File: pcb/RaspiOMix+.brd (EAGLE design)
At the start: 65 x 56 mm, 103 parts, among them IC3 DS1307, IC4 MCP3424-E/ST, IC5 MCP3424-E/ST, IC6 TMP101, K1 PIN20X2, U1 EEPROM24

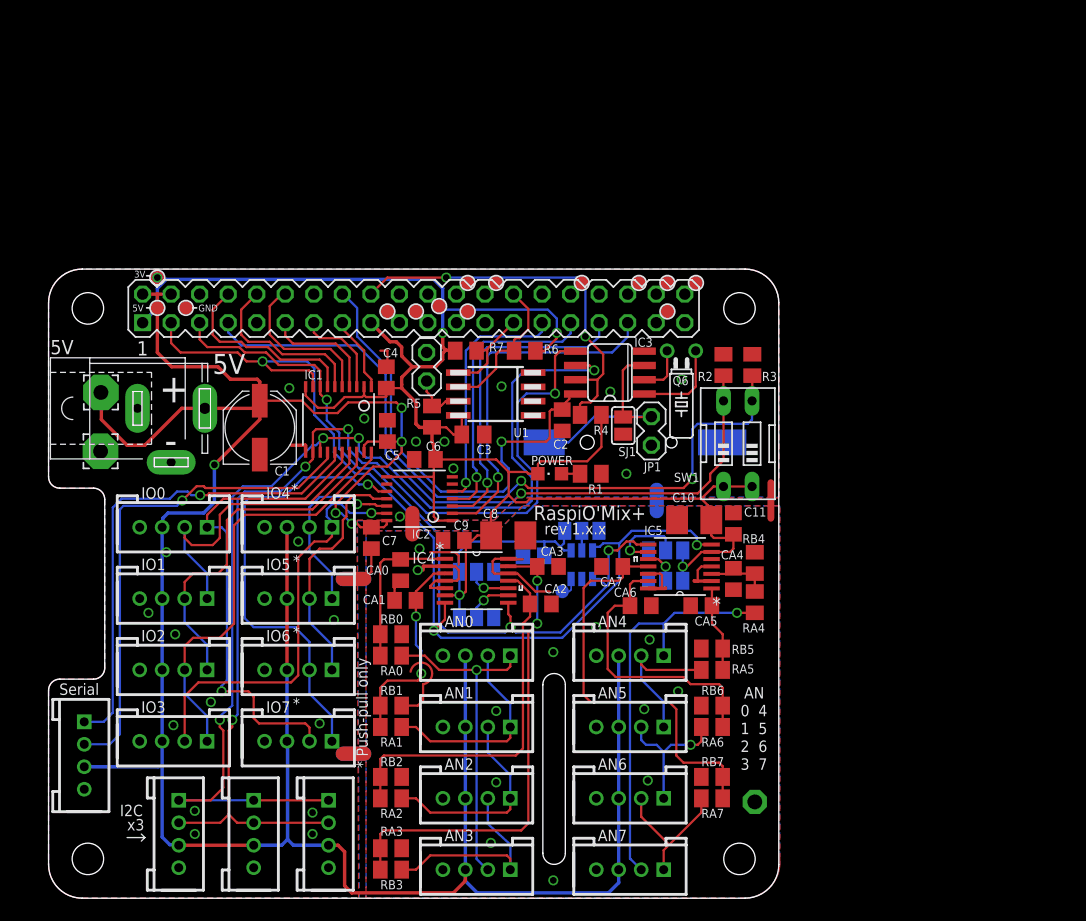
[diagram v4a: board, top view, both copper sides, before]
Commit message: RaspiO'Mix+ -> Pcb 2.0.0
New RaspiO’Mix+ pcbs version is 2.0.0.
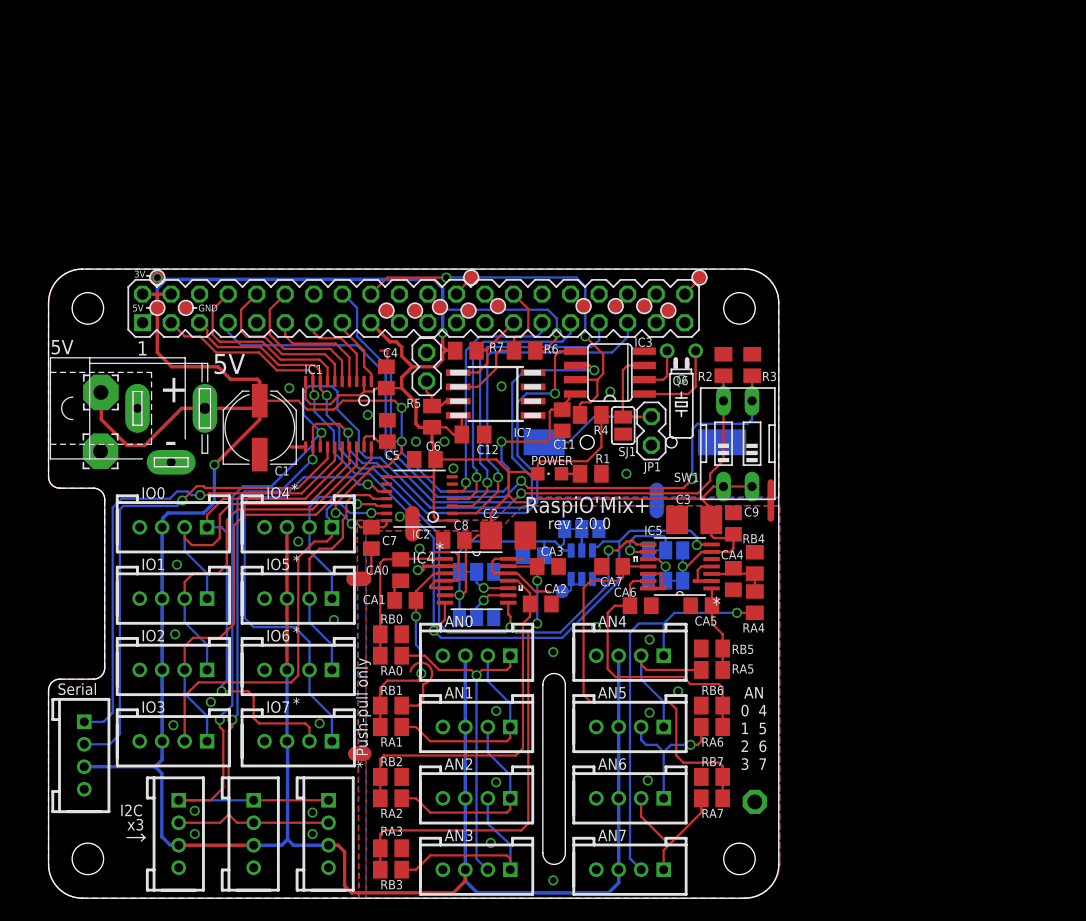
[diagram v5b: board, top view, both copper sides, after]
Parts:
- C10, C8: value (none) -> 100nf; device rcl:B/3528-21R -> rcl:C0805
- C12: device rcl:C0805 -> resistor:C0805K
- C2: value 100nf -> 1uf; device rcl:C0805 -> rcl:B/3528-21R
- C3: value 100nF -> 1uf; device resistor:C0805K -> rcl:B/3528-21R
- IC1: value (none) -> TXS0108PWR
- IC2: value (none) -> TXB0104PWR
- Q6: value (none) -> 32.768khz
- moved C9 24.9 mm to (61.0, 33.3), turned to 270 degrees
- moved C3 21.1 mm to (57.5, 33.7)
- moved C11 17.8 mm to (45.7, 42.5)
- moved C10 14.6 mm to (43.2, 30.5), flipped to the bottom
- moved C12 12.1 mm to (37.8, 41.3), flipped to the top
- moved C2 11.3 mm to (40.9, 32.3), turned to 180 degrees
- moved C8 4.87 mm to (36.1, 31.8), turned to 0 degrees
- moved TP3 2.92 mm to (53.0, 52.7)
- moved TP4 2.92 mm to (50.5, 52.7)
- moved TP9 2.07 mm to (40.0, 52.7)
- moved TP5 2.07 mm to (47.6, 52.7)
- moved TP2 0.57 mm to (57.9, 55.2)
- moved TP8 0.57 mm to (37.6, 55.2)
- moved IC1 0.48 mm to (25.8, 43.1)
- moved J_ADR4 0.16 mm to (47.5, 32.9)
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- renumbered U1 to IC7
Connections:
- net +3V3: now also C10.1, C2.+, C3.+, C8.2; no longer C10.+, C11.2, C3.1, C8.+
- net +5V: now also C11.1; no longer C2.1
- net VSS: now also C10.2, C11.2, C2.-, C3.-, C8.1; no longer C10.-, C11.1, C2.2, C3.2, C8.-
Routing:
- net SCL: track 99.1 -> 108.4 mm, vias 4 -> 3
- net PI_SDA: track 87.6 -> 80.3 mm
- net VSS: track 59.1 -> 54.6 mm, vias 34 -> 33
- net N$28: track 0.00 -> 0.79 mm
- net N$27: track 0.00 -> 0.79 mm
- net PI_RX: track 15.6 -> 15.0 mm
- net PI_IO0: track 14.1 -> 13.4 mm
- net N$23: track 0.00 -> 0.64 mm
- net N$26: track 0.00 -> 0.63 mm
- net N$25: track 0.00 -> 0.63 mm
- net N$24: track 0.00 -> 0.63 mm
- net N$1: track 1.41 -> 2.02 mm
- net PI_SCL: track 69.4 -> 68.8 mm
- net N$16: track 1.41 -> 1.98 mm
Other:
- board text added: "rev 2.0.0"
- board text removed: "rev 1.x.x"

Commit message: Misc
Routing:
- net VSS: vias 33 -> 34
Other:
- board text added: "rev 2.0.1"
- board text removed: "rev 2.0.0"
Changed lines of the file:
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@@
 <text x="63.1825" y="13.0175" size="1.016" layer="21" font="vector">6</text>
 <text x="63.1825" y="11.43" size="1.016" layer="21" font="vector">7</text>
-<text x="44.45" y="32.86125" size="1.016" layer="21" font="vector">rev 2.0.0</text>
+<text x="44.45" y="32.86125" size="1.016" layer="21" font="vector">rev 2.0.1</text>
 <text x="31.59125" y="48.5775" size="1.4224" layer="26" font="vector" rot="MR0">www.digitalspirit.org</text>
 <text x="31.59125" y="46.355" size="1.27" layer="26" font="vector" rot="MR0">2014/11</text>
@@
 <circle x="57.94375" y="55.245" radius="0.654540625" width="0.1524" layer="21"/>
 <circle x="55.165625" y="52.308125" radius="0.654540625" width="0.1524" layer="21"/>
+<circle x="36.67125" y="30.00375" radius="0.15875" width="0.4064" layer="21"/>
+<circle x="57.62625" y="27.78125" radius="0.15875" width="0.4064" layer="21"/>
+<circle x="51.1175" y="45.085" radius="0.15875" width="0.4064" layer="21"/>
 </plain>
 <attributes>
@@
 </element>
 <element name="RA3" library="rcl" package="M0805" value="10k 0.1%" x="30.48" y="2.54" smashed="yes">
-<attribute name="NAME" x="29.5275" y="5.55625" size="0.8128" layer="25"/>
+<attribute name="NAME" x="29.36875" y="0.635" size="0.8128" layer="25"/>
 <attribute name="VALUE" x="29.21" y="0" size="1.27" layer="27"/>
 </element>
@@
 </element>
 <element name="RB3" library="rcl" package="M0805" value="6.8k 1%" x="30.48" y="4.445" smashed="yes" rot="R180">
-<attribute name="NAME" x="29.5275" y="0.79375" size="0.8128" layer="25" rot="R180" align="top-right"/>
+<attribute name="NAME" x="29.5275" y="5.55625" size="0.8128" layer="25" rot="R180" align="top-right"/>
 <attribute name="VALUE" x="31.75" y="6.985" size="1.27" layer="27" rot="R180"/>
 </element>
@@
 <wire x1="40.48125" y1="36.195" x2="40.9575" y2="36.67125" width="0.2032" layer="16"/>
 <wire x1="40.9575" y1="36.67125" x2="40.9575" y2="38.25875" width="0.2032" layer="16"/>
-<wire x1="40.9575" y1="38.25875" x2="40.3225" y2="38.89375" width="0.2032" layer="16"/>
-<wire x1="40.3225" y1="38.89375" x2="40.3225" y2="40.64" width="0.2032" layer="16"/>
-<via x="40.3225" y="40.64" extent="1-16" drill="0.6"/>
-<wire x1="40.3225" y1="40.64" x2="44.29125" y2="40.64" width="0.2032" layer="1"/>
+<wire x1="40.9575" y1="38.25875" x2="40.16375" y2="39.0525" width="0.2032" layer="16"/>
+<wire x1="40.16375" y1="39.0525" x2="40.16375" y2="40.64" width="0.2032" layer="16"/>
+<via x="40.16375" y="40.64" extent="1-16" drill="0.6"/>
+<wire x1="40.16375" y1="40.64" x2="44.29125" y2="40.64" width="0.2032" layer="1"/>
 <wire x1="44.29125" y1="40.64" x2="44.60875" y2="40.9575" width="0.2032" layer="1"/>
 <wire x1="44.60875" y1="40.9575" x2="44.60875" y2="43.33875" width="0.2032" layer="1"/>
@@
 <via x="13.0175" y="5.715" extent="1-16" drill="0.6"/>
 <via x="14.44625" y="17.4625" extent="1-16" drill="0.6"/>
+<via x="55.40375" y="26.3525" extent="1-16" drill="0.6"/>
 <wire x1="40.9194" y1="28.9179" x2="40.9575" y2="28.8925" width="0" layer="19" extent="1-1"/>
 <wire x1="39.624" y1="29.05125" x2="39.52875" y2="29.05125" width="0" layer="19" extent="1-16"/>
-<wire x1="53.3781" y1="28.8671" x2="53.4035" y2="28.2575" width="0" layer="19" extent="1-16"/>
 </signal>
 <signal name="SDA">
@@
 <wire x1="45.085" y1="44.92625" x2="42.545" y2="44.92625" width="0.2032" layer="16"/>
 <wire x1="42.545" y1="44.92625" x2="41.75125" y2="44.1325" width="0.2032" layer="16"/>
-<wire x1="41.75125" y1="44.1325" x2="41.75125" y2="39.37" width="0.2032" layer="16"/>
-<wire x1="41.75125" y1="39.37" x2="43.4975" y2="37.62375" width="0.2032" layer="16"/>
+<wire x1="41.75125" y1="44.1325" x2="41.75125" y2="42.38625" width="0.2032" layer="16"/>
+<wire x1="41.75125" y1="42.38625" x2="41.43375" y2="42.06875" width="0.2032" layer="16"/>
+<wire x1="41.43375" y1="42.06875" x2="41.43375" y2="39.6875" width="0.2032" layer="16"/>
+<wire x1="41.43375" y1="39.6875" x2="43.4975" y2="37.62375" width="0.2032" layer="16"/>
 <wire x1="43.4975" y1="37.62375" x2="43.4975" y2="35.2425" width="0.2032" layer="16"/>
 <wire x1="43.4975" y1="35.2425" x2="42.545" y2="34.29" width="0.2032" layer="16"/>
@@
 <wire x1="48.5775" y1="46.99" x2="42.38625" y2="46.99" width="0.2032" layer="16"/>
 <wire x1="42.38625" y1="46.99" x2="41.275" y2="45.87875" width="0.2032" layer="16"/>
-<wire x1="41.275" y1="45.87875" x2="41.275" y2="39.21125" width="0.2032" layer="16"/>
-<wire x1="41.275" y1="39.21125" x2="43.02125" y2="37.465" width="0.2032" layer="16"/>
+<wire x1="41.275" y1="45.87875" x2="41.275" y2="42.545" width="0.2032" layer="16"/>
+<wire x1="41.275" y1="42.545" x2="40.9575" y2="42.2275" width="0.2032" layer="16"/>
+<wire x1="40.9575" y1="42.2275" x2="40.9575" y2="41.5925" width="0.2032" layer="16"/>
+<wire x1="40.9575" y1="41.5925" x2="40.9575" y2="39.52875" width="0.2032" layer="16"/>
+<wire x1="40.9575" y1="39.52875" x2="43.02125" y2="37.465" width="0.2032" layer="16"/>
 <wire x1="43.02125" y1="37.465" x2="43.02125" y2="35.40125" width="0.2032" layer="16"/>
 <wire x1="43.02125" y1="35.40125" x2="42.38625" y2="34.76625" width="0.2032" layer="16"/>

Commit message: PCB Version 2.0.2
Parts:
- moved C3 0.22 mm to (57.3, 33.8)
- moved C6 0.16 mm to (33.5, 39.2)
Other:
- board text added: "rev 2.0.2"
- board text removed: "rev 2.0.1"
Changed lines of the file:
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@@
 <?xml version="1.0" encoding="utf-8"?>
 <!DOCTYPE eagle SYSTEM "eagle.dtd">
-<eagle version="7.2.0">
+<eagle version="7.3.0">
 <drawing>
 <settings>
@@
 <text x="63.1825" y="13.0175" size="1.016" layer="21" font="vector">6</text>
 <text x="63.1825" y="11.43" size="1.016" layer="21" font="vector">7</text>
-<text x="44.45" y="32.86125" size="1.016" layer="21" font="vector">rev 2.0.1</text>
+<text x="44.45" y="32.86125" size="1.016" layer="21" font="vector">rev 2.0.2</text>
 <text x="31.59125" y="48.5775" size="1.4224" layer="26" font="vector" rot="MR0">www.digitalspirit.org</text>
 <text x="31.59125" y="46.355" size="1.27" layer="26" font="vector" rot="MR0">2014/11</text>
@@
 <text x="19.3675" y="0.635" size="1.016" layer="22" font="vector" rot="MR0">I2C</text>
 <text x="25.7175" y="0.635" size="1.016" layer="22" font="vector" rot="MR0">I2C</text>
-<text x="9.8425" y="2.2225" size="1.016" layer="22" font="vector" rot="MR0">SCL</text>
-<text x="9.8425" y="4.1275" size="1.016" layer="22" font="vector" rot="MR0">SDA</text>
+<text x="9.8425" y="8.255" size="1.016" layer="22" font="vector" rot="MR0">SCL</text>
+<text x="9.8425" y="6.35" size="1.016" layer="22" font="vector" rot="MR0">SDA</text>
 <text x="5.87375" y="13.335" size="1.016" layer="22" font="vector" rot="MR0">TX</text>
 <text x="5.87375" y="15.24" size="1.016" layer="22" font="vector" rot="MR0">RX</text>
@@
 <attribute name="VALUE" x="54.8274" y="30.95625" size="0.02" layer="28" rot="MR180"/>
 </element>
-<element name="C3" library="rcl" package="B/3528-21R" value="1uf" x="57.4675" y="33.655" smashed="yes">
-<attribute name="NAME" x="55.835" y="35.09625" size="0.8128" layer="25"/>
-<attribute name="VALUE" x="55.5175" y="30.73" size="1.27" layer="27"/>
+<element name="C3" library="rcl" package="B/3528-21R" value="1uf" x="57.30875" y="33.81375" smashed="yes">
+<attribute name="NAME" x="55.67625" y="35.255" size="0.8128" layer="25"/>
+<attribute name="VALUE" x="55.35875" y="30.88875" size="1.27" layer="27"/>
 </element>
 <element name="IC2" library="adafruit" package="TSSOP14" value="TXB0104PWR" x="33.02" y="35.56" smashed="yes" rot="R90">
@@
 <attribute name="VALUE" x="26.19375" y="33.3375" size="1.27" layer="27" rot="R270"/>
 </element>
-<element name="C6" library="rcl" package="C0805" value="100nf" x="33.49625" y="39.0525" smashed="yes" rot="R180">
-<attribute name="NAME" x="34.925" y="40.64" size="0.8128" layer="25" rot="R180"/>
-<attribute name="VALUE" x="34.76625" y="41.5925" size="1.27" layer="27" rot="R180"/>
+<element name="C6" library="rcl" package="C0805" value="100nf" x="33.49625" y="39.21125" smashed="yes" rot="R180">
+<attribute name="NAME" x="34.925" y="40.79875" size="0.8128" layer="25" rot="R180"/>
+<attribute name="VALUE" x="34.76625" y="41.75125" size="1.27" layer="27" rot="R180"/>
 </element>
 <element name="JP1" library="FLYFISH" package="PIN_W_2" value="" x="53.6575" y="40.3225" smashed="yes" rot="R180">
@@
 <wire x1="43.33625" y1="48.73625" x2="44.08625" y2="48.69" width="0.2032" layer="1"/>
 <wire x1="44.08625" y1="48.69" x2="45.24375" y2="49.8475" width="0.2032" layer="1"/>
-<wire x1="34.44625" y1="39.0525" x2="34.29" y2="39.0525" width="0.2032" layer="1"/>
+<wire x1="34.44625" y1="39.21125" x2="34.29" y2="39.0525" width="0.2032" layer="1"/>
 <wire x1="59.0169" y1="30.8229" x2="60.6679" y2="30.8229" width="0.2032" layer="1"/>
 <wire x1="36.576" y1="26.9875" x2="36.576" y2="29.05125" width="0.2032" layer="16"/>
@@
 <wire x1="34.29" y1="55.08625" x2="35.08375" y2="54.2925" width="0.3048" layer="16"/>
 <wire x1="35.08375" y1="54.2925" x2="35.08375" y2="50.32375" width="0.3048" layer="16"/>
-<wire x1="34.44625" y1="39.0525" x2="39.84625" y2="39.0525" width="0.2032" layer="1"/>
-<wire x1="39.84625" y1="39.0525" x2="40.9575" y2="37.94125" width="0.2032" layer="1"/>
+<wire x1="34.44625" y1="39.21125" x2="38.735" y2="39.21125" width="0.2032" layer="1"/>
+<wire x1="38.735" y1="39.21125" x2="39.52875" y2="38.4175" width="0.2032" layer="1"/>
+<wire x1="39.52875" y1="38.4175" x2="40.48125" y2="38.4175" width="0.2032" layer="1"/>
+<wire x1="40.48125" y1="38.4175" x2="40.9575" y2="37.94125" width="0.2032" layer="1"/>
 <wire x1="43.55875" y1="37.7825" x2="43.55875" y2="38.6375" width="0.2032" layer="1"/>
 <wire x1="43.55875" y1="38.6375" x2="43.815" y2="38.89375" width="0.2032" layer="1"/>
@@
 <wire x1="60.08" y1="36.6475" x2="59.19" y2="36.6475" width="0.2032" layer="1"/>
 <wire x1="59.19" y1="36.6475" x2="58.1025" y2="35.56" width="0.2032" layer="1"/>
-<wire x1="58.9925" y1="33.655" x2="58.7375" y2="33.655" width="0.2032" layer="1"/>
+<wire x1="58.83375" y1="33.81375" x2="58.7375" y2="33.655" width="0.2032" layer="1"/>
 <wire x1="58.7375" y1="33.655" x2="58.675" y2="33.7175" width="0.2032" layer="1"/>
 <wire x1="58.675" y1="33.7175" x2="58.675" y2="34.9875" width="0.2032" layer="1"/>
@@
 <wire x1="47.9425" y1="38.89375" x2="49.21" y2="40.16125" width="0.2032" layer="1"/>
 <wire x1="60.6679" y1="30.8229" x2="60.96" y2="31.115" width="0.2032" layer="1"/>
-<wire x1="58.9925" y1="33.655" x2="58.9925" y2="32.28875" width="0.2032" layer="1"/>
+<wire x1="58.83375" y1="33.81375" x2="58.9925" y2="32.28875" width="0.2032" layer="1"/>
 <wire x1="58.9925" y1="32.28875" x2="59.21375" y2="32.0675" width="0.2032" layer="1"/>
 <wire x1="59.21375" y1="32.0675" x2="60.9575" y2="32.0675" width="0.2032" layer="1"/>
